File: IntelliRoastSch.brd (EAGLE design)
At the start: 53.3 x 94.5 mm, 28 parts, among them U1 LM2576HVS-3.3/NOPB

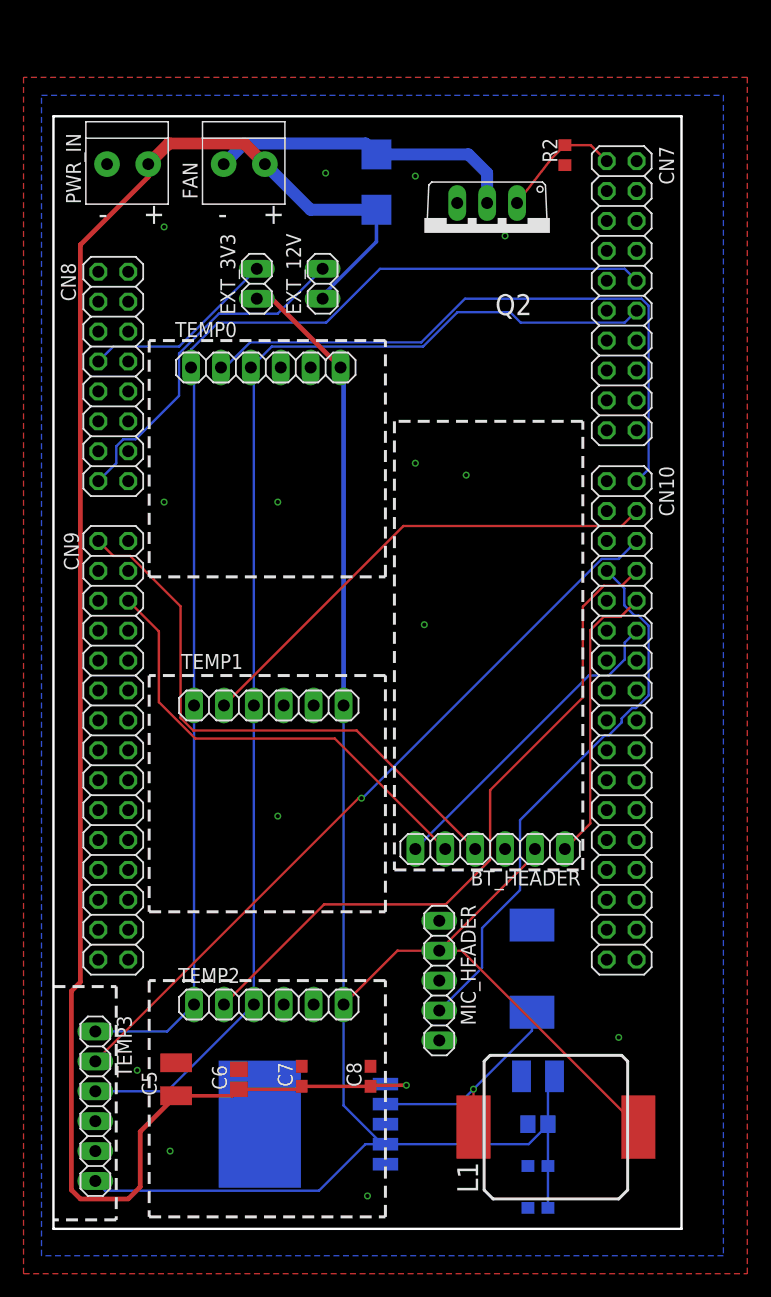
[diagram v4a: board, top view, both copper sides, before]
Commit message: Moved Mic Header and tried to straighten up some of the traces. Don't think I actually helped anything.
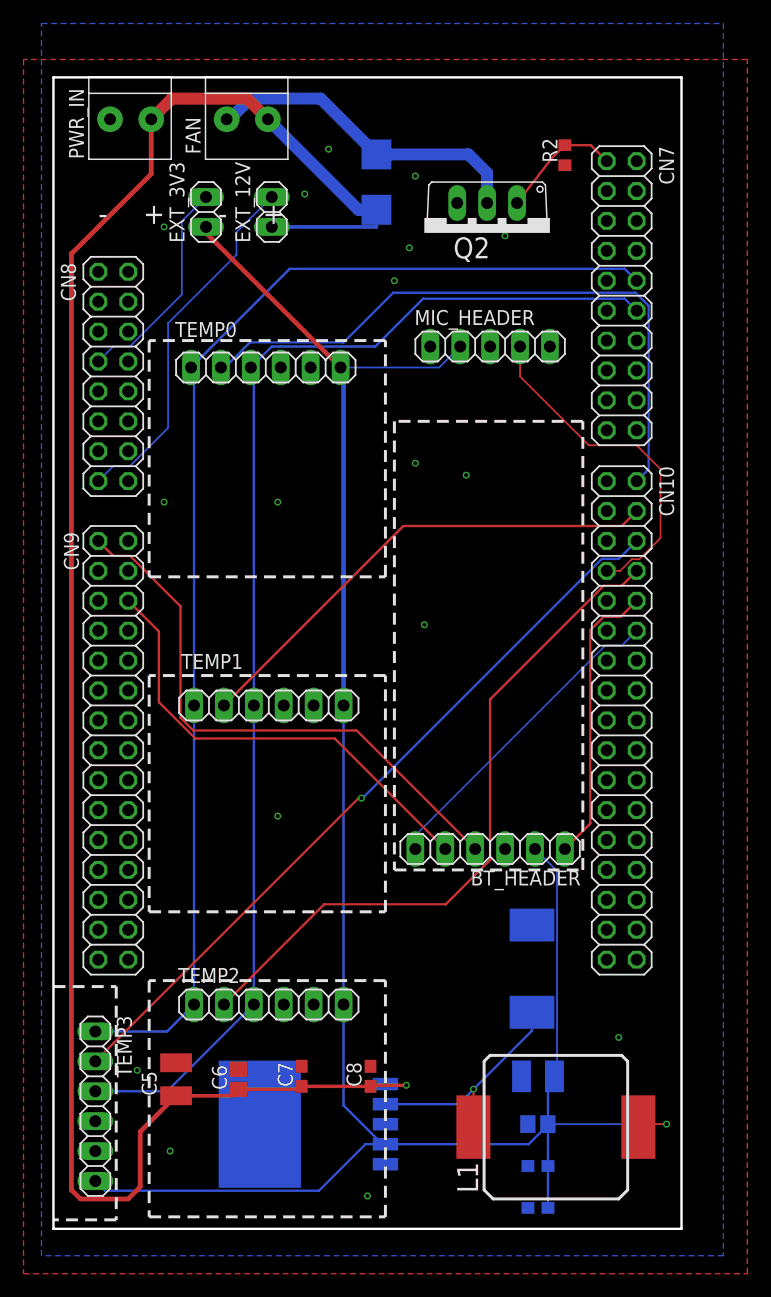
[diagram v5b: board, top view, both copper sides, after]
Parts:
- moved MIC_HEADER 54.0 mm to (37.1, 54.6), turned to 0 degrees
- moved EXT_12V 7.47 mm to (18.5, 66.0)
- moved EXT_3V3 7.47 mm to (13.0, 66.0)
- moved FAN 3.82 mm to (16.5, 73.9)
- moved PWR_IN 3.82 mm to (6.60, 73.9)
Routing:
- net MIC_IN: track 46.8 -> 29.3 mm
- net +12V: track 159.0 -> 165.2 mm
- net +3V3: track 174.9 -> 180.6 mm, vias 0 -> 1
- net N$2: track 16.7 -> 18.6 mm
- net N$3: track 29.5 -> 31.1 mm
- net FAN_TO_MOS: track 26.7 -> 28.0 mm
- net SPI1_SCK: track 106.2 -> 105.3 mm
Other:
- board size 53.3 x 94.5 mm -> 53.3 x 97.8 mm

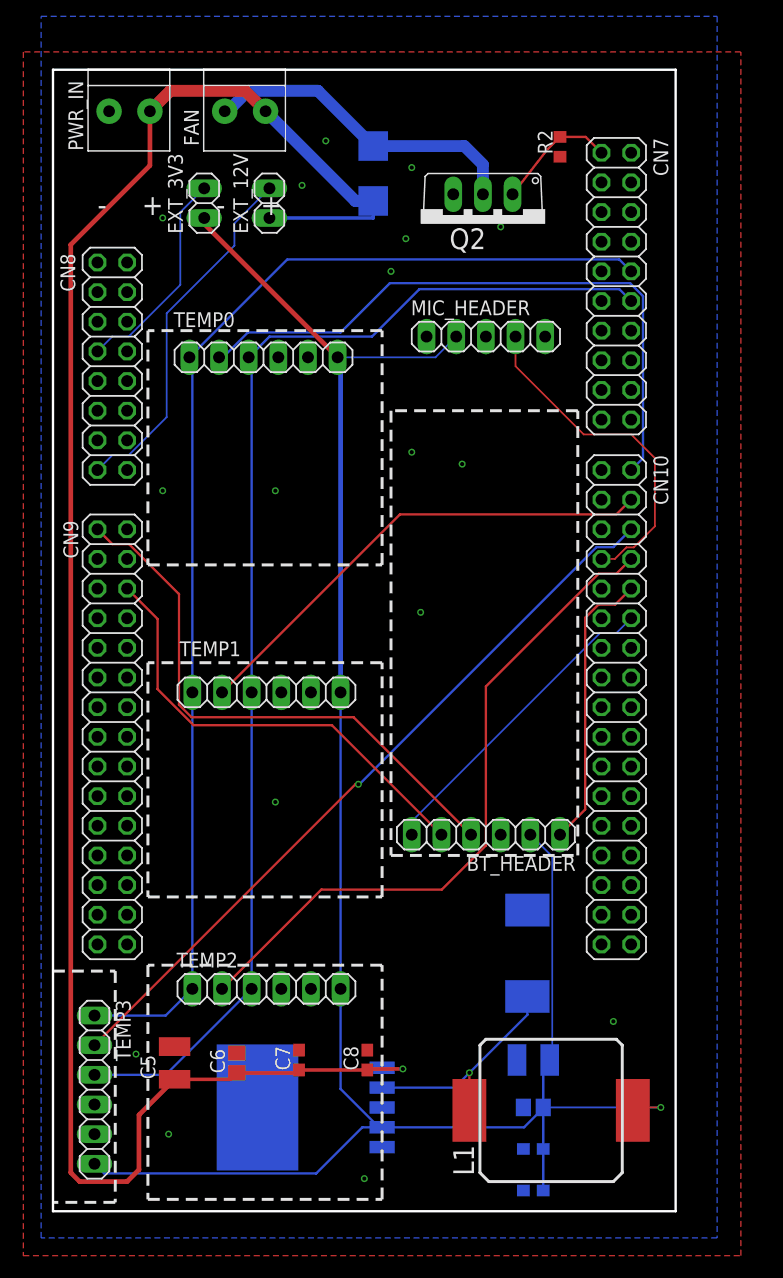
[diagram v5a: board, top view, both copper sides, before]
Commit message: Redid the board. Should have better tolorences and the traces are better laid out. Need to add 0Ω resistors on all the connections if we need to change things around.
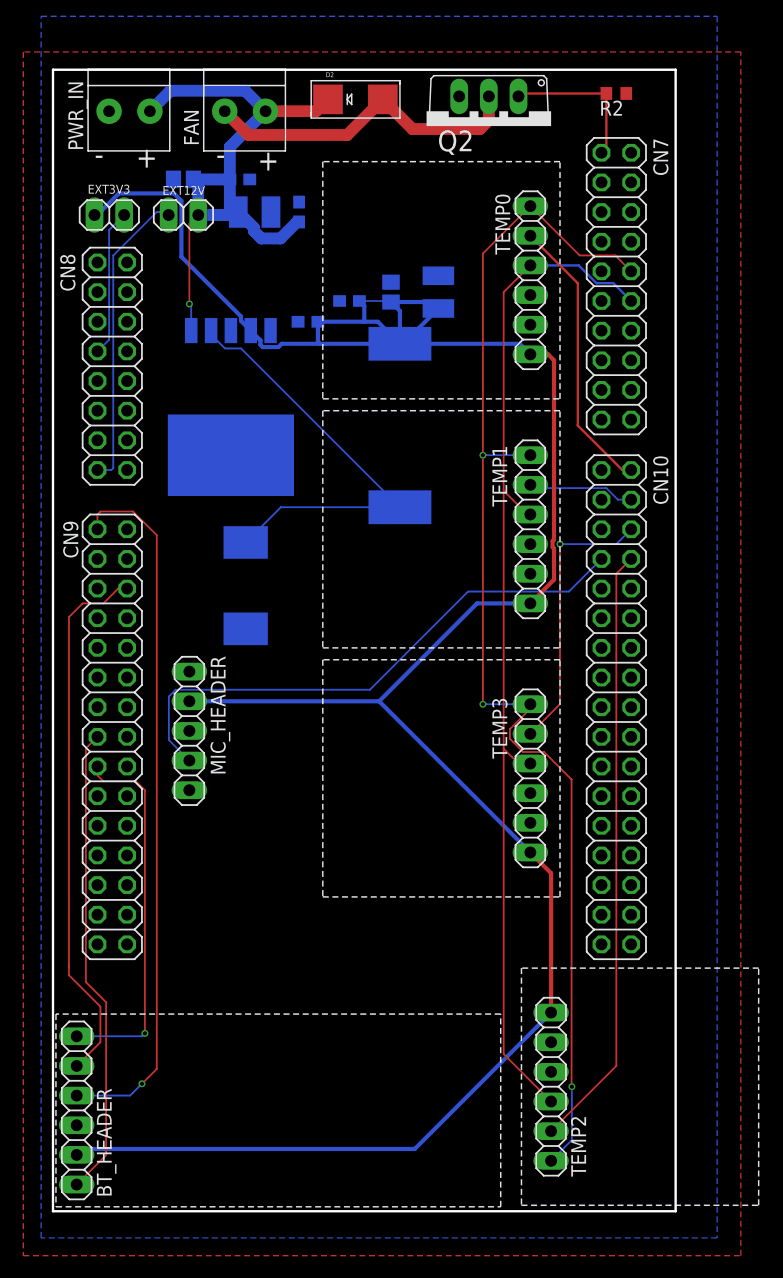
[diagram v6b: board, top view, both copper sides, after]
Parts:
- removed EXT_12V, EXT_3V3: (no value), pinhead:1X02
- added EXT12V, EXT3V3: (no value), pinhead:1X02
- BT_HEADER: device pinhead:1X06 -> IntelliRoast:HC-O5_HEADER
- TEMP0, TEMP1, TEMP2, TEMP3: device pinhead:1X06 -> IntelliRoast:MAX31855_HEADER
- moved C4 76.9 mm to (21.8, 55.9)
- moved C8 76.2 mm to (16.0, 68.1), flipped to the bottom, turned to 180 degrees
- moved C6 75.8 mm to (11.2, 68.1), flipped to the bottom, turned to 0 degrees
- moved C3 74.3 mm to (25.4, 57.7)
- moved C5 73.2 mm to (17.3, 65.3), flipped to the bottom, turned to 180 degrees
- moved C7 72.6 mm to (21.1, 65.3), flipped to the bottom
- moved C2 70.9 mm to (29.0, 58.4), turned to 90 degrees
- moved C1 66.3 mm to (33.0, 58.4), turned to 90 degrees
- moved U1 61.7 mm to (15.2, 49.8), turned to 270 degrees
- moved L1 60.1 mm to (29.7, 47.0), flipped to the bottom, turned to 180 degrees
- moved TEMP3 45.9 mm to (40.9, 16.8)
- moved BT_HEADER 42.3 mm to (2.03, -11.7), turned to 90 degrees
- moved MIC_HEADER 42.3 mm to (11.7, 20.8), turned to 270 degrees
- moved D1 39.7 mm to (16.5, 33.3), turned to 270 degrees
- moved TEMP1 26.6 mm to (40.9, 38.1), turned to 270 degrees
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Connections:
- net +12V: now also EXT12V.1; no longer EXT_12V.1
- net +3V3: now also EXT3V3.1; no longer EXT_3V3.1
- net BT_ENABLE: now also CN9.15; no longer CN10.10
- net BT_STATE: now also CN9.17; no longer CN10.12
- net N$2: now also EXT3V3.2; no longer EXT_3V3.2
- net N$3: now also EXT12V.2; no longer EXT_12V.2
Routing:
- net +12V: track 165.2 -> 54.5 mm
- net SPI1_CS3: track 64.3 -> 23.9 mm
- net SPI2_CS1: track 41.9 -> 9.16 mm
- net SPI2_CS0: track 54.7 -> 24.1 mm
- net +3V3: track 180.6 -> 209.7 mm, vias 1 -> 0
- net MIC_IN: track 29.3 -> 48.2 mm
- net OUT: track 19.8 -> 37.1 mm, vias 1 -> 0
- net SPI1_MISO: track 106.3 -> 90.1 mm
- net BT_ENABLE: track 24.4 -> 40.5 mm
- net BT_RX: track 48.4 -> 60.8 mm, vias 0 -> 1
- net BT_TX: track 39.2 -> 46.4 mm
- net SPI1_CS2: track 58.3 -> 51.9 mm
- net N$2: track 18.6 -> 12.6 mm
- net N$3: track 31.1 -> 26.0 mm
- net BT_STATE: track 27.1 -> 32.1 mm, vias 0 -> 1
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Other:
- board text removed: "L1"

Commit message: added zero ohms
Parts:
- added R3, R4, R5, R6, SPI_CLK, SPI_MISO: 0, SparkFun-Resistors:0603
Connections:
- new net SPI1_CS2_RES: R6.2, TEMP2.2
- new net SPI1_CS3_RES: R5.2, TEMP3.2
- new net SPI2_CS0_RES: R3.2, TEMP0.2
- new net SPI2_CS1_RES: R4.2, TEMP1.2
- new net SPI_BUS_CLK: SPI_CLK.2, TEMP0.1, TEMP1.1, TEMP2.1, TEMP3.1
- new net SPI_BUS_MISO: SPI_MISO.2, TEMP0.3, TEMP1.3, TEMP2.3, TEMP3.3
- net SPI1_CS2: now also R6.1; no longer TEMP2.2
- net SPI1_CS3: now also R5.1; no longer TEMP3.2
- net SPI1_MISO: now also SPI_MISO.1; no longer TEMP0.3, TEMP1.3, TEMP2.3, TEMP3.3
- net SPI1_SCK: now also SPI_CLK.1; no longer TEMP0.1, TEMP1.1, TEMP2.1, TEMP3.1
- net SPI2_CS0: now also R3.1; no longer TEMP0.2
- net SPI2_CS1: now also R4.1; no longer TEMP1.2
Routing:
- net SPI_BUS_CLK: track 0.00 -> 97.8 mm, vias 0 -> 3
- net SPI1_SCK: track 107.3 -> 12.8 mm, vias 3 -> 0
- net SPI_BUS_MISO: track 0.00 -> 89.7 mm, vias 0 -> 1
- net SPI1_MISO: track 90.1 -> 17.5 mm, vias 0 -> 1
- net SPI1_CS2: track 51.9 -> 0.00 mm
- net SPI1_CS2_RES: track 0.00 -> 50.1 mm
- net SPI2_CS0: track 24.1 -> 0.00 mm
- net SPI1_CS3: track 23.9 -> 0.00 mm, vias 1 -> 0
- net SPI2_CS0_RES: track 0.00 -> 23.3 mm
- net SPI1_CS3_RES: track 0.00 -> 22.1 mm, vias 0 -> 1
- net SPI2_CS1: track 9.16 -> 0.00 mm
- net SPI2_CS1_RES: track 0.00 -> 8.02 mm
